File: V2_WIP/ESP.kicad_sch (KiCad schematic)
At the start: 40 parts, among them J3 BATT, P1 USB_C_Plug_USB2.0, Q1 IRLML5203, Q2 S8050, Q3 S8050, SW3 SW_Push, SW4 SW_Push, U1 ESP32-WROOM-32E, U12 RT9742AGJ5F, U13 TP4057, U14 CH340K

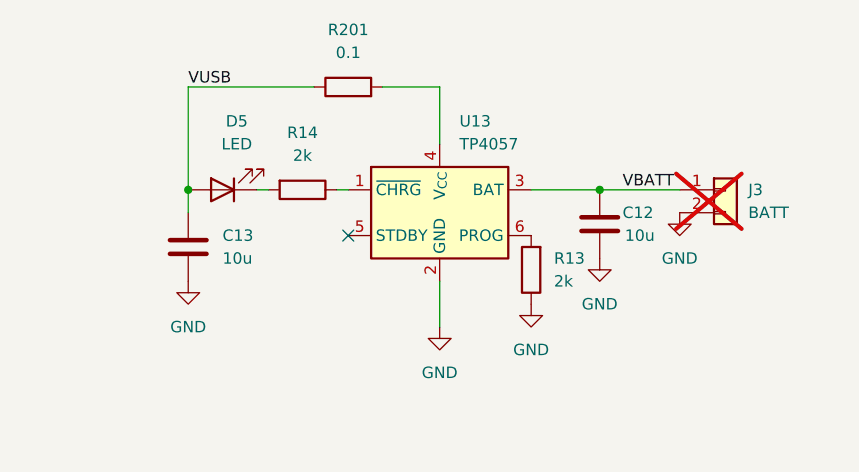
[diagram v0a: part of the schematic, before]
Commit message: added FLASH module; moved encoder into separate schematic
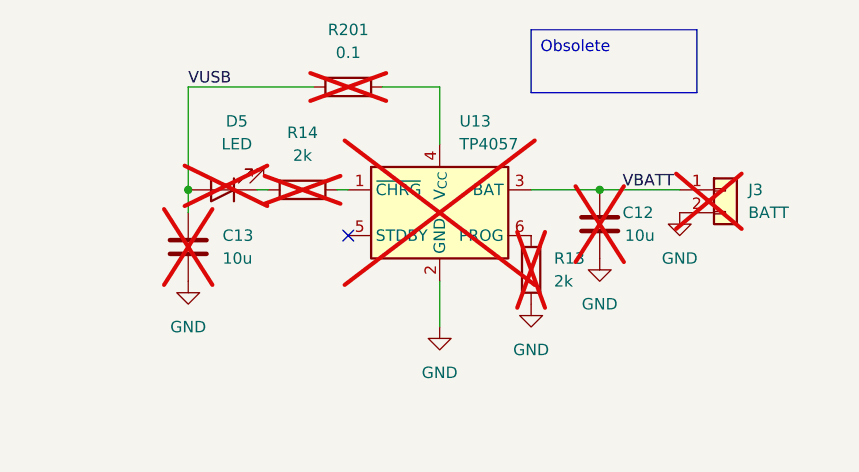
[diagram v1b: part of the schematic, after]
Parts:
- C12, C13, D5, R13, R14, R201, U13: now not fitted
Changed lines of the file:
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@@
 		)
 	)
+	(text_box "Obsolete"
+		(exclude_from_sim no)
+		(at 154.94 19.05 0)
+		(size 18.415 6.985)
+		(stroke
+			(width 0)
+			(type default)
+		)
+		(fill
+			(type none)
+		)
+		(effects
+			(font
+				(size 1.27 1.27)
+			)
+			(justify left top)
+		)
+	)
 	(text "Wrong footprint"
 		(exclude_from_sim no)
@@
 		(exclude_from_sim no)
 		(in_bom yes)
-		(on_board yes)
-		(dnp no)
+		(on_board no)
+		(dnp yes)
 		(fields_autoplaced yes)
 		(property "Reference" "C13"
@@
 		(exclude_from_sim no)
 		(in_bom yes)
-		(on_board yes)
-		(dnp no)
+		(on_board no)
+		(dnp yes)
 		(fields_autoplaced yes)
 		(property "Reference" "R201"
@@
 		(exclude_from_sim no)
 		(in_bom yes)
-		(on_board yes)
-		(dnp no)
+		(on_board no)
+		(dnp yes)
 		(fields_autoplaced yes)
 		(property "Reference" "D5"
@@
 		(exclude_from_sim no)
 		(in_bom yes)
-		(on_board yes)
-		(dnp no)
+		(on_board no)
+		(dnp yes)
 		(fields_autoplaced yes)
 		(property "Reference" "U13"
@@
 		(exclude_from_sim no)
 		(in_bom yes)
-		(on_board yes)
-		(dnp no)
+		(on_board no)
+		(dnp yes)
 		(property "Reference" "C12"
 			(at 165.1 39.37 0)
@@
 		(exclude_from_sim no)
 		(in_bom yes)
-		(on_board yes)
-		(dnp no)
+		(on_board no)
+		(dnp yes)
 		(fields_autoplaced yes)
 		(property "Reference" "R13"
@@
 		(exclude_from_sim no)
 		(in_bom yes)
-		(on_board yes)
-		(dnp no)
+		(on_board no)
+		(dnp yes)
 		(fields_autoplaced yes)
 		(property "Reference" "R14"

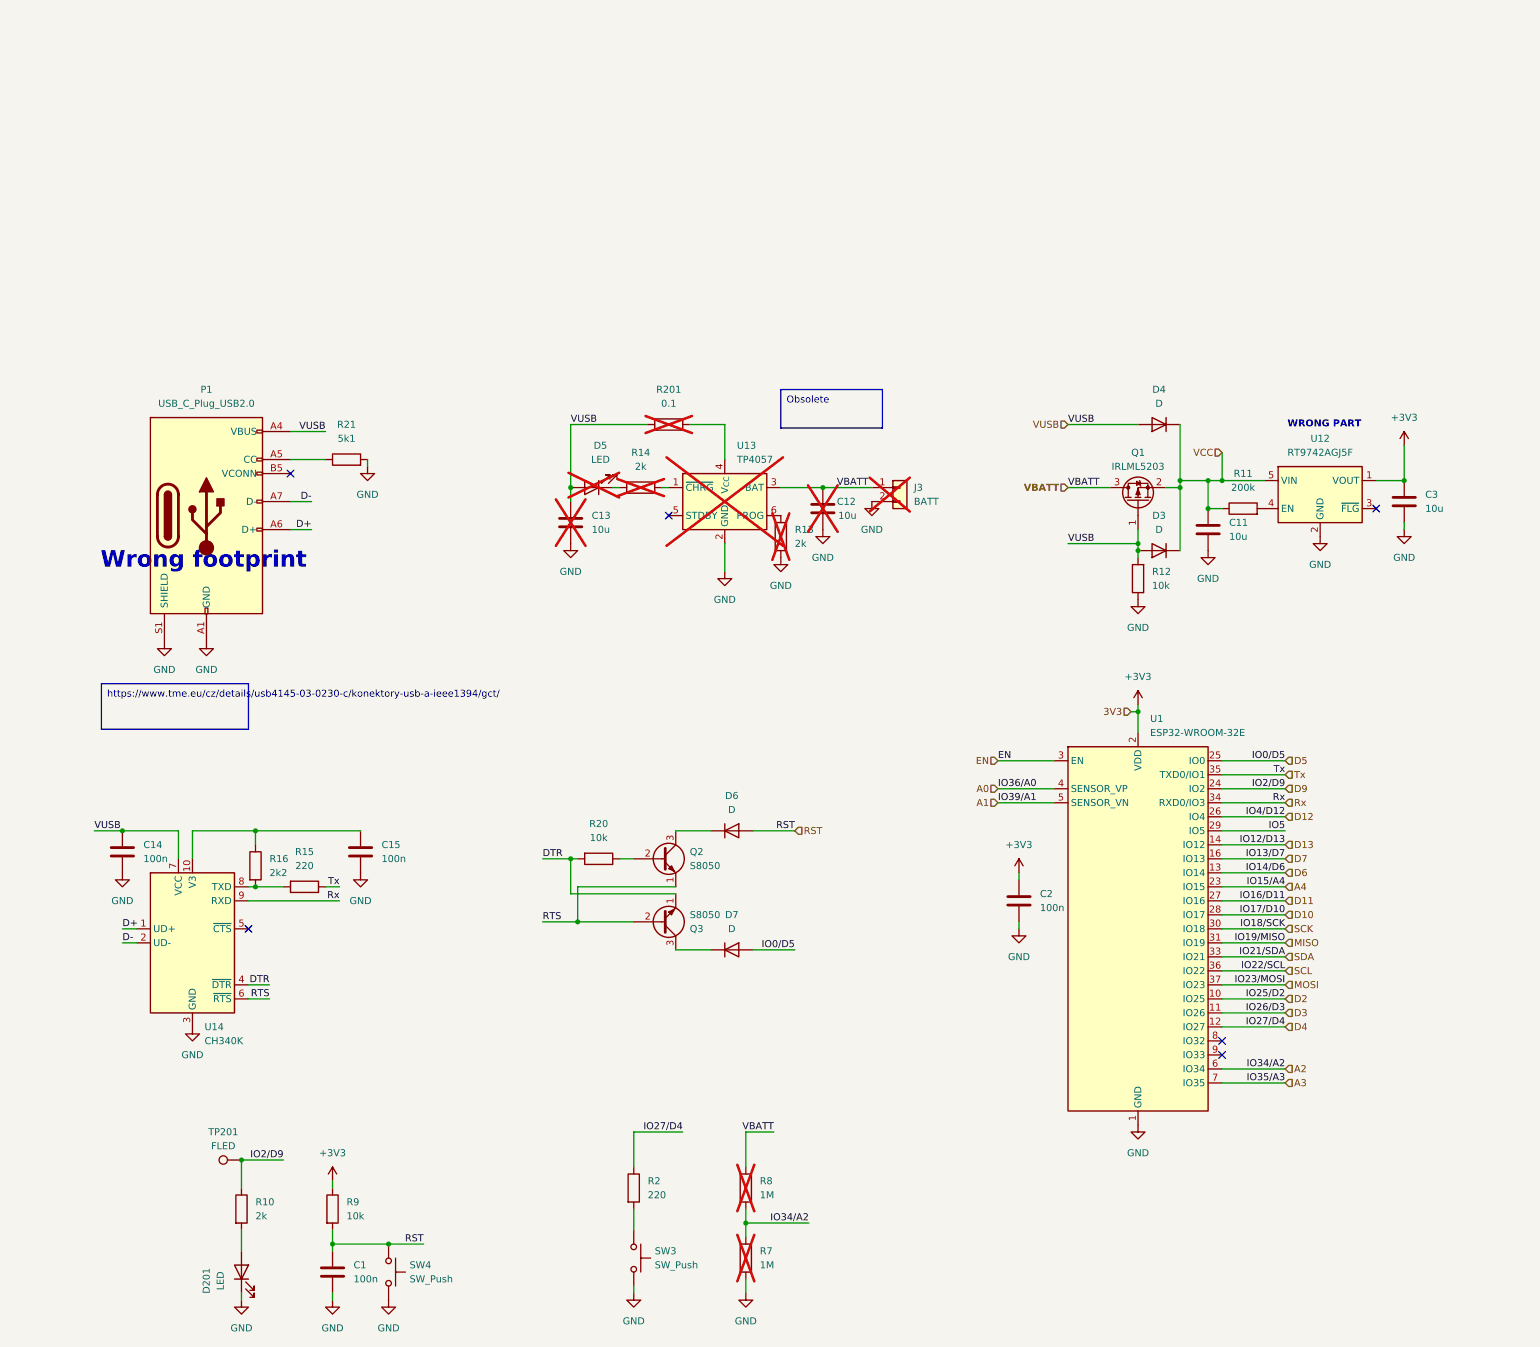
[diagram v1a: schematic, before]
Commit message: added USB, button
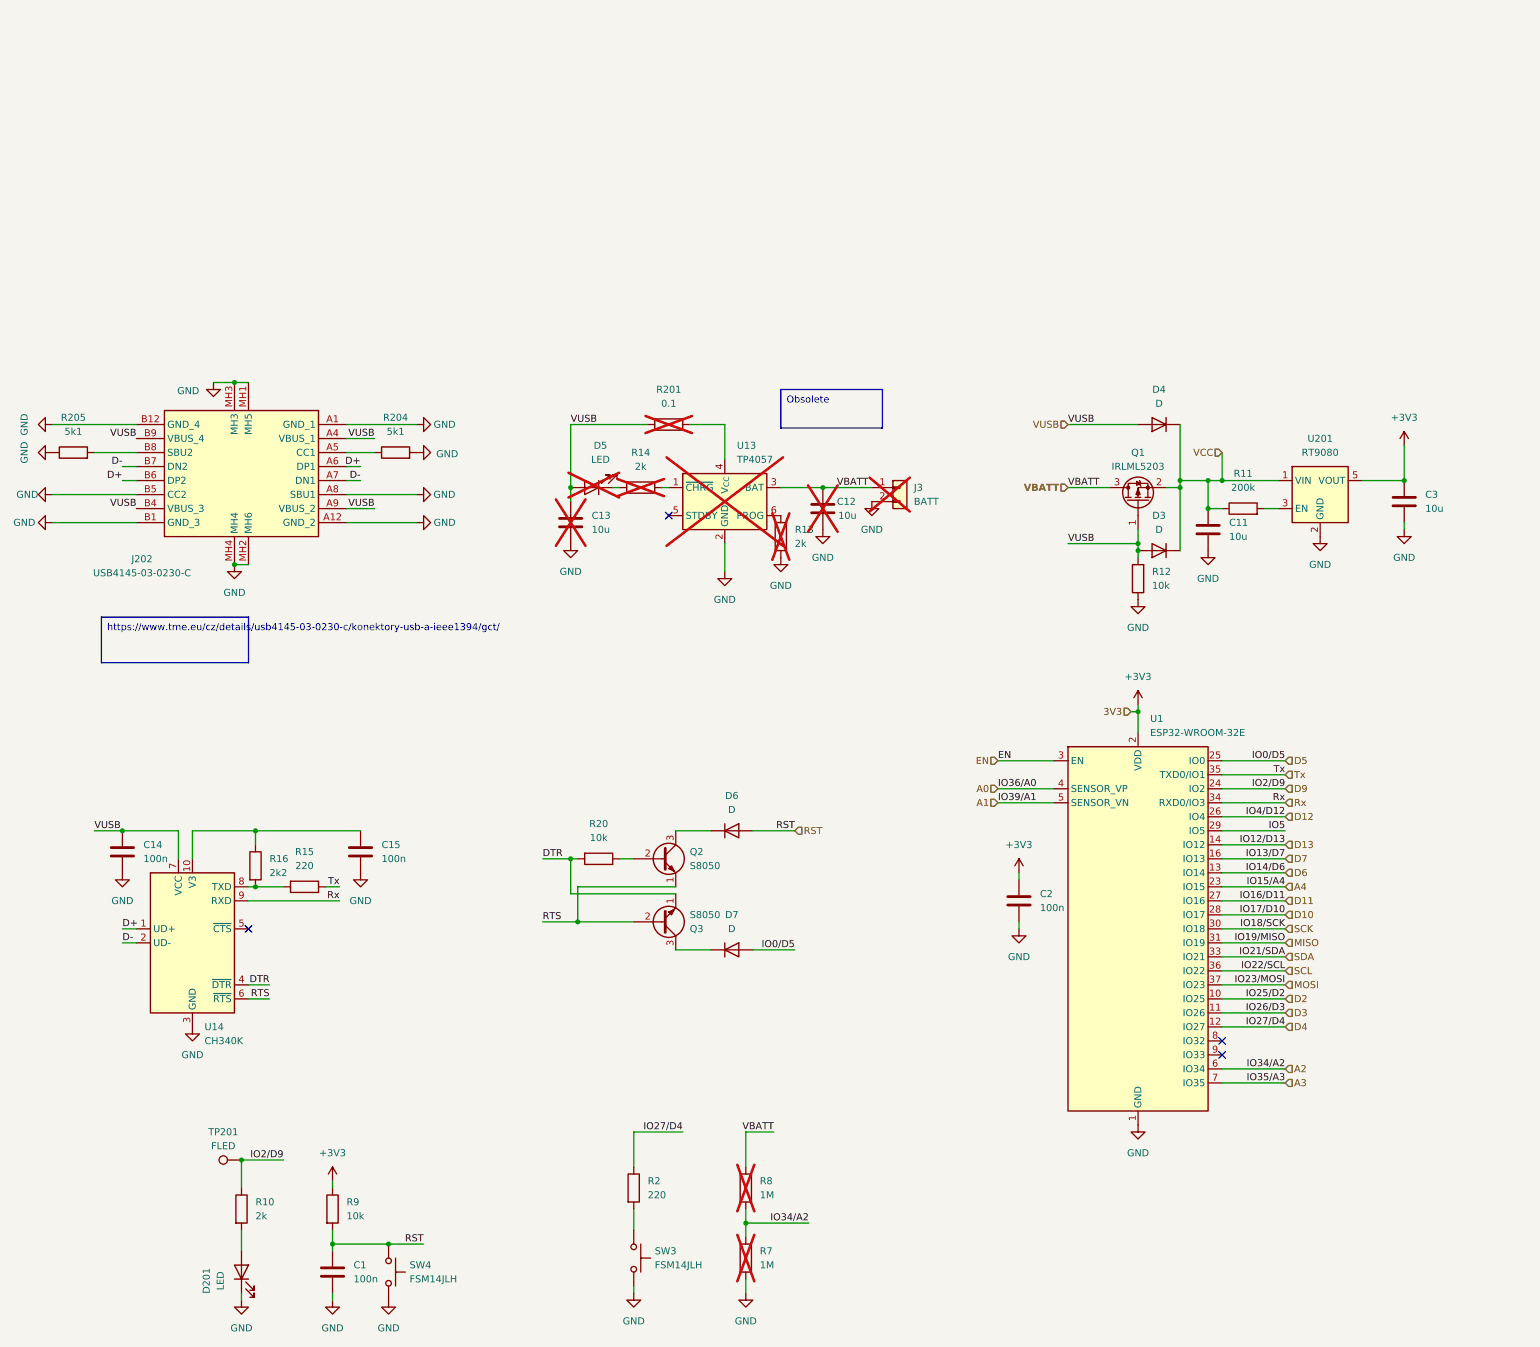
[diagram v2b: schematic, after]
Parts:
- removed P1: USB_C_Plug_USB2.0, Connector_USB:USB_C_Receptacle_G-Switch_GT-USB-7051x, symbol Connector:USB_C_Plug_USB2.0
- removed R21: 5k1, Resistor_SMD:R_0603_1608Metric_Pad0.98x0.95mm_HandSolder, symbol Device:R
- removed U12: RT9742AGJ5F, Package_TO_SOT_SMD:TSOT-23-5, symbol Power_Management:RT9742AGJ5F
- added J202: USB4145-03-0230-C, KiCad:USB4145030230C, symbol USB4145-03-0230-C:USB4145-03-0230-C
- added R204, R205: 5k1, Resistor_SMD:R_0603_1608Metric_Pad0.98x0.95mm_HandSolder, symbol Device:R
- added U201: RT9080, Package_TO_SOT_SMD:SOT-23-5_HandSoldering, symbol Regulator_Linear:NCP163ASN500T1G
- SW3, SW4: value SW_Push -> FSM14JLH
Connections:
- net +3V3: now also U201.5 (VOUT)
- net D+: now also J202.A6 (DP1), J202.B6 (DP2)
- net D-: now also J202.A7 (DN1), J202.B7 (DN2)
- net GND: now also J202.A1 (GND_1), J202.A12 (GND_2), J202.A8 (SBU1), J202.B1 (GND_3), J202.B12 (GND_4), J202.B5 (CC2), J202.MH1 (MH5), J202.MH2 (MH6), J202.MH3, J202.MH4, R204.2, R205.1, U201.2 (GND)
- net VCC: now also U201.1 (VIN)
- net VUSB: now also J202.A4 (VBUS_1), J202.A9 (VBUS_2), J202.B4 (VBUS_3), J202.B9 (VBUS_4)
- net at R11.2: now also U201.3 (EN)
- new net: J202.A5 (CC1), R204.1
- new net: J202.B8 (SBU2), R205.2
- no-connect marks 6 -> 4
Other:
- note removed: "WRONG PART"
- note removed: "Wrong footprint"

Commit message: fixed errors in schematic
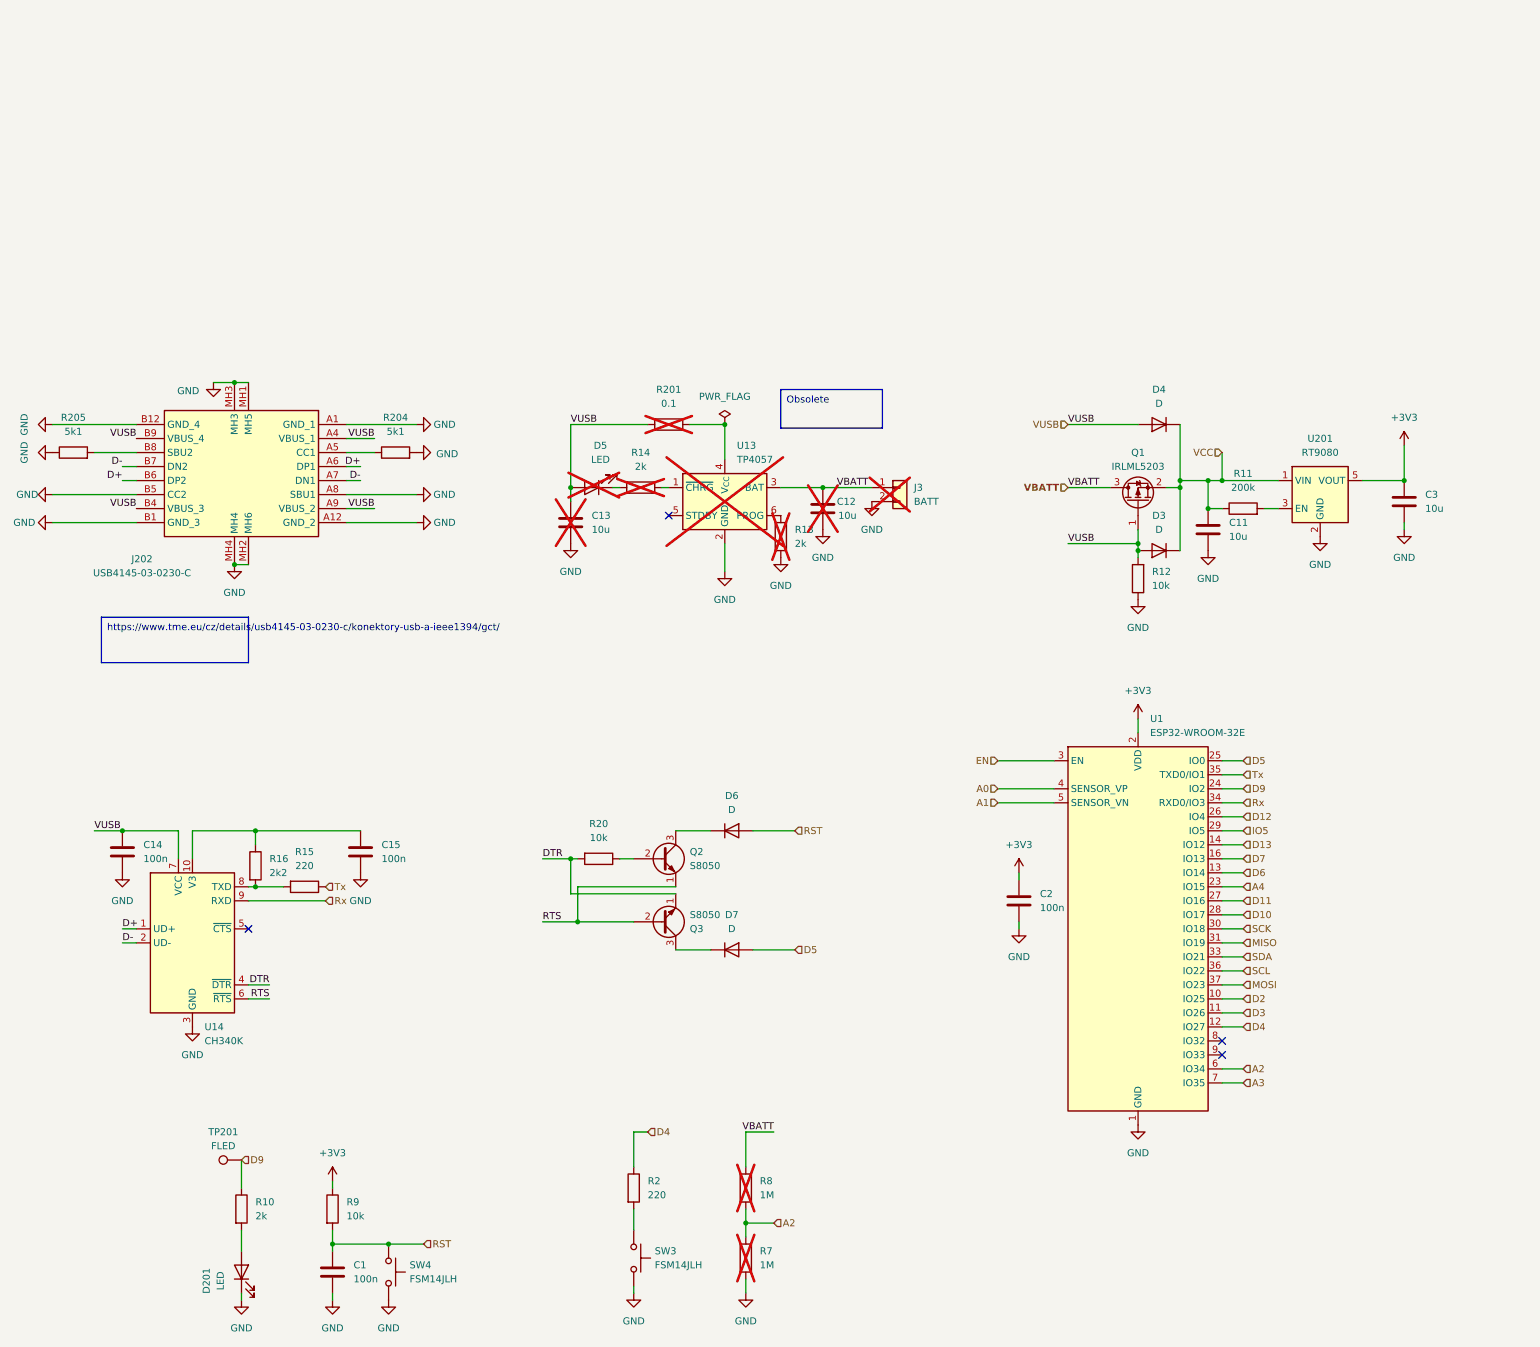
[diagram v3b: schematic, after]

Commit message: schematic tweaks
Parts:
- U1: footprint RF_Module:ESP32-WROOM-32D -> RF_Module:ESP32-WROOM-32UE
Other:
- moved on the sheet: C12, C13, D5, J3, R13, R14, R201, U13
